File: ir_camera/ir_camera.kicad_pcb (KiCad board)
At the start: 2 copper layers, 43.6 x 54.3 mm, 23 parts, among them J1 PowerIn, J2 Screen, U1 L7805, U2 ATMEGA328P-PU, U3 LD1117, U4 pixart_ir, Y1 Crystal_4pin, Y2 Crystal

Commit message: IR Camera v0.2
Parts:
- moved R1 7.53 mm to (180.0, 72.9), turned to -90 degrees
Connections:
- U4 pad 5: SLC -> SCL
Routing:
- net SCL: track 45.4 -> 75.1 mm
- net 4.5V: track 103.9 -> 97.7 mm
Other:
- board text added: "IR Camera v0.2 M.I.A.R. Labs nick.groesz@gmail.com"
- board text removed: "IR Camera v0.1 M.I.A.R. Labs nick.groesz@gmail.com"
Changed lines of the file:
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@@
 	(net 29 "unconnected-(U2-(PCINT4{slash}MISO)PB4-Pad18)")
 	(net 30 "unconnected-(U4-NC-Pad4)")
-	(net 31 "SLC")
-	(net 32 "Net-(U4-CLK)")
-	(net 33 "unconnected-(Y1-NC-Pad1)")
+	(net 31 "Net-(U4-CLK)")
+	(net 32 "unconnected-(Y1-NC-Pad1)")
 	(footprint "custom:pixart_ir"
 		(layer "F.Cu")
@@
 			(layers "*.Cu" "*.Mask")
 			(remove_unused_layers no)
-			(net 31 "SLC")
+			(net 8 "SCL")
 			(pinfunction "SLC")
 			(pintype "input")
@@
 			(layers "*.Cu" "*.Mask")
 			(remove_unused_layers no)
-			(net 32 "Net-(U4-CLK)")
+			(net 31 "Net-(U4-CLK)")
 			(pinfunction "CLK")
 			(pintype "input")
@@
 	(footprint "Resistor_THT:R_Axial_DIN0207_L6.3mm_D2.5mm_P7.62mm_Horizontal"
 		(layer "F.Cu")
-		(at 180.7 80.4 90)
+		(at 180 72.9 -90)
 		(descr "Resistor, Axial_DIN0207 series, Axial, Horizontal, pin pitch=7.62mm, 0.25W = 1/4W, length*diameter=6.3*2.5mm^2, http://cdn-reichelt.de/documents/datenblatt/B400/1_4W%23YAG.pdf")
 		(tags "Resistor Axial_DIN0207 series Axial Horizontal pin pitch 7.62mm 0.25W = 1/4W length 6.3mm diameter 2.5mm")
@@
 		)
 		(property "Datasheet" ""
-			(at 0 0 90)
+			(at 0 0 270)
 			(unlocked yes)
 			(layer "F.Fab")
@@
 		)
 		(property "Description" ""
-			(at 0 0 90)
+			(at 0 0 270)
 			(unlocked yes)
 			(layer "F.Fab")
@@
 		(attr through_hole)
 		(fp_line
-			(start 7.08 -1.37)
-			(end 7.08 -1.04)
+			(start 0.54 1.37)
+			(end 7.08 1.37)
 			(stroke
 				(width 0.12)
@@
 		)
 		(fp_line
-			(start 0.54 -1.37)
-			(end 7.08 -1.37)
+			(start 7.08 1.37)
+			(end 7.08 1.04)
 			(stroke
 				(width 0.12)
@@
 		)
 		(fp_line
-			(start 0.54 -1.04)
-			(end 0.54 -1.37)
+			(start 0.54 1.04)
+			(end 0.54 1.37)
 			(stroke
 				(width 0.12)
@@
 		)
 		(fp_line
-			(start 0.54 1.04)
-			(end 0.54 1.37)
+			(start 0.54 -1.04)
+			(end 0.54 -1.37)
 			(stroke
 				(width 0.12)
@@
 		)
 		(fp_line
-			(start 7.08 1.37)
-			(end 7.08 1.04)
+			(start 0.54 -1.37)
+			(end 7.08 -1.37)
 			(stroke
 				(width 0.12)
@@
 		)
 		(fp_line
-			(start 0.54 1.37)
-			(end 7.08 1.37)
+			(start 7.08 -1.37)
+			(end 7.08 -1.04)
 			(stroke
 				(width 0.12)
@@
 		)
 		(fp_line
-			(start 8.67 -1.5)
-			(end -1.05 -1.5)
+			(start -1.05 1.5)
+			(end 8.67 1.5)
 			(stroke
 				(width 0.05)
@@
 		)
 		(fp_line
-			(start -1.05 -1.5)
-			(end -1.05 1.5)
+			(start 8.67 1.5)
+			(end 8.67 -1.5)
 			(stroke
 				(width 0.05)
@@
 		)
 		(fp_line
-			(start 8.67 1.5)
-			(end 8.67 -1.5)
+			(start -1.05 -1.5)
+			(end -1.05 1.5)
 			(stroke
 				(width 0.05)
@@
 		)
 		(fp_line
-			(start -1.05 1.5)
-			(end 8.67 1.5)
+			(start 8.67 -1.5)
+			(end -1.05 -1.5)
 			(stroke
 				(width 0.05)
@@
 		)
 		(fp_line
-			(start 6.96 -1.25)
-			(end 0.66 -1.25)
+			(start 0.66 1.25)
+			(end 6.96 1.25)
 			(stroke
 				(width 0.1)
@@
 		)
 		(fp_line
-			(start 0.66 -1.25)
-			(end 0.66 1.25)
+			(start 6.96 1.25)
+			(end 6.96 -1.25)
 			(stroke
 				(width 0.1)
@@
 		)
 		(fp_line
-			(start 7.62 0)
-			(end 6.96 0)
+			(start 0 0)
+			(end 0.66 0)
 			(stroke
 				(width 0.1)
@@
 		)
 		(fp_line
-			(start 0 0)
-			(end 0.66 0)
+			(start 7.62 0)
+			(end 6.96 0)
 			(stroke
 				(width 0.1)
@@
 		)
 		(fp_line
-			(start 6.96 1.25)
-			(end 6.96 -1.25)
+			(start 0.66 -1.25)
+			(end 0.66 1.25)
 			(stroke
 				(width 0.1)
@@
 		)
 		(fp_line
-			(start 0.66 1.25)
-			(end 6.96 1.25)
+			(start 6.96 -1.25)
+			(end 0.66 -1.25)
 			(stroke
 				(width 0.1)
@@
 		)
 		(pad "1" thru_hole circle
-			(at 0 0 90)
+			(at 0 0 270)
 			(size 1.6 1.6)
 			(drill 0.8)
@@
 		)
 		(pad "2" thru_hole oval
-			(at 7.62 0 90)
+			(at 7.62 0 270)
 			(size 1.6 1.6)
 			(drill 0.8)
@@
 			(layers "*.Cu" "*.Mask")
 			(remove_unused_layers no)
-			(net 33 "unconnected-(Y1-NC-Pad1)")
+			(net 32 "unconnected-(Y1-NC-Pad1)")
 			(pinfunction "NC")
 			(pintype "passive+no_connect")
@@
 			(layers "*.Cu" "*.Mask")
 			(remove_unused_layers no)
-			(net 32 "Net-(U4-CLK)")
+			(net 31 "Net-(U4-CLK)")
 			(pinfunction "Output")
 			(pintype "passive")
@@
 		(layer "Edge.Cuts")
 	)
-	(gr_text "IR Camera v0.1\nM.I.A.R. Labs\nnick.groesz@gmail.com"
+	(gr_text "IR Camera v0.2\nM.I.A.R. Labs\nnick.groesz@gmail.com"
 		(at 169.5 79.3 90)
 		(layer "B.SilkS")
@@
 	)
 	(segment
-		(start 145.85 98.77)
-		(end 145.85 99)
-		(width 0.2)
-		(layer "F.Cu")
-		(net 2)
-	)
-	(segment
 		(start 159.1 114.5)
 		(end 159.8 113.8)
@@
 	)
 	(segment
-		(start 176.3 97.3)
-		(end 176.3 88)
+		(start 176.8 80.52)
+		(end 180 80.52)
 		(width 0.2)
 		(layer "B.Cu")
@@
 	)
 	(segment
-		(start 163.799 103.701)
-		(end 165 102.5)
+		(start 176.3 97.3)
+		(end 176.3 88)
 		(width 0.2)
 		(layer "B.Cu")
@@
 	)
 	(segment
-		(start 176.8 80.52)
-		(end 176.8 76.68)
+		(start 163.799 103.701)
+		(end 165 102.5)
 		(width 0.2)
 		(layer "B.Cu")
@@
 	)
 	(segment
-		(start 176.8 76.68)
-		(end 180.7 72.78)
-		(width 0.2)
-		(layer "B.Cu")
-		(net 3)
-	)
-	(segment
 		(start 153.58295 84.1)
 		(end 158.73295 89.25)
@@
 	)
 	(segment
-		(start 177.901 80.06395)
-		(end 177.901 80.15)
+		(start 163.183 67.6758)
+		(end 162.582 67.0748)
 		(width 0.2)
 		(layer "F.Cu")
@@
 	)
 	(segment
-		(start 180.45 80.15)
-		(end 180.7 80.4)
+		(start 174.8661 79.651)
+		(end 180 74.5171)
 		(width 0.2)
 		(layer "F.Cu")
@@
 	)
 	(segment
-		(start 176.34395 79.419)
-		(end 177.25605 79.419)
+		(start 163.391 79.651)
+		(end 174.8661 79.651)
 		(width 0.2)
 		(layer "F.Cu")
@@
 	)
 	(segment
-		(start 163.89 80.15)
-		(end 175.699 80.15)
+		(start 174.7758 67.6758)
+		(end 163.183 67.6758)
 		(width 0.2)
 		(layer "F.Cu")
@@
 	)
 	(segment
-		(start 177.25605 79.419)
-		(end 177.901 80.06395)
+		(start 180 72.9)
+		(end 174.7758 67.6758)
 		(width 0.2)
 		(layer "F.Cu")
@@
 	)
 	(segment
-		(start 175.699 80.06395)
-		(end 176.34395 79.419)
-		(width 0.2)
-		(layer "F.Cu")
-		(net 8)
-	)
-	(segment
-		(start 175.699 80.15)
-		(end 175.699 80.06395)
-		(width 0.2)
-		(layer "F.Cu")
-		(net 8)
-	)
-	(segment
-		(start 177.901 80.15)
-		(end 180.45 80.15)
+		(start 159.1 75.36)
+		(end 163.391 79.651)
 		(width 0.2)
 		(layer "F.Cu")
@@
 	)
 	(segment
-		(start 159.1 75.36)
-		(end 163.89 80.15)
+		(start 180 74.5171)
+		(end 180 72.9)
 		(width 0.2)
 		(layer "F.Cu")
@@
 	)
 	(segment
-		(start 181.499999 81.199999)
-		(end 181.499999 98.400001)
+		(start 181.5 74.4)
+		(end 180 72.9)
 		(width 0.2)
 		(layer "B.Cu")
@@
 	)
 	(segment
-		(start 180.7 80.4)
-		(end 181.499999 81.199999)
+		(start 181.5 98.4)
+		(end 181.5 74.4)
 		(width 0.2)
 		(layer "B.Cu")
@@
 	)
 	(segment
-		(start 181.499999 98.400001)
-		(end 179.6 100.3)
+		(start 179.6 100.3)
+		(end 181.5 98.4)
 		(width 0.2)
 		(layer "B.Cu")
@@
 		(width 0.2)
 		(layer "B.Cu")
-		(net 32)
+		(net 31)
 	)
 	(segment
@@
 		(width 0.2)
 		(layer "B.Cu")
-		(net 32)
+		(net 31)
 	)
 	(segment
@@
 		(width 0.2)
 		(layer "B.Cu")
-		(net 32)
+		(net 31)
 	)
 	(segment
@@
 		(width 0.2)
 		(layer "B.Cu")
-		(net 32)
+		(net 31)
 	)
 	(embedded_fonts no)

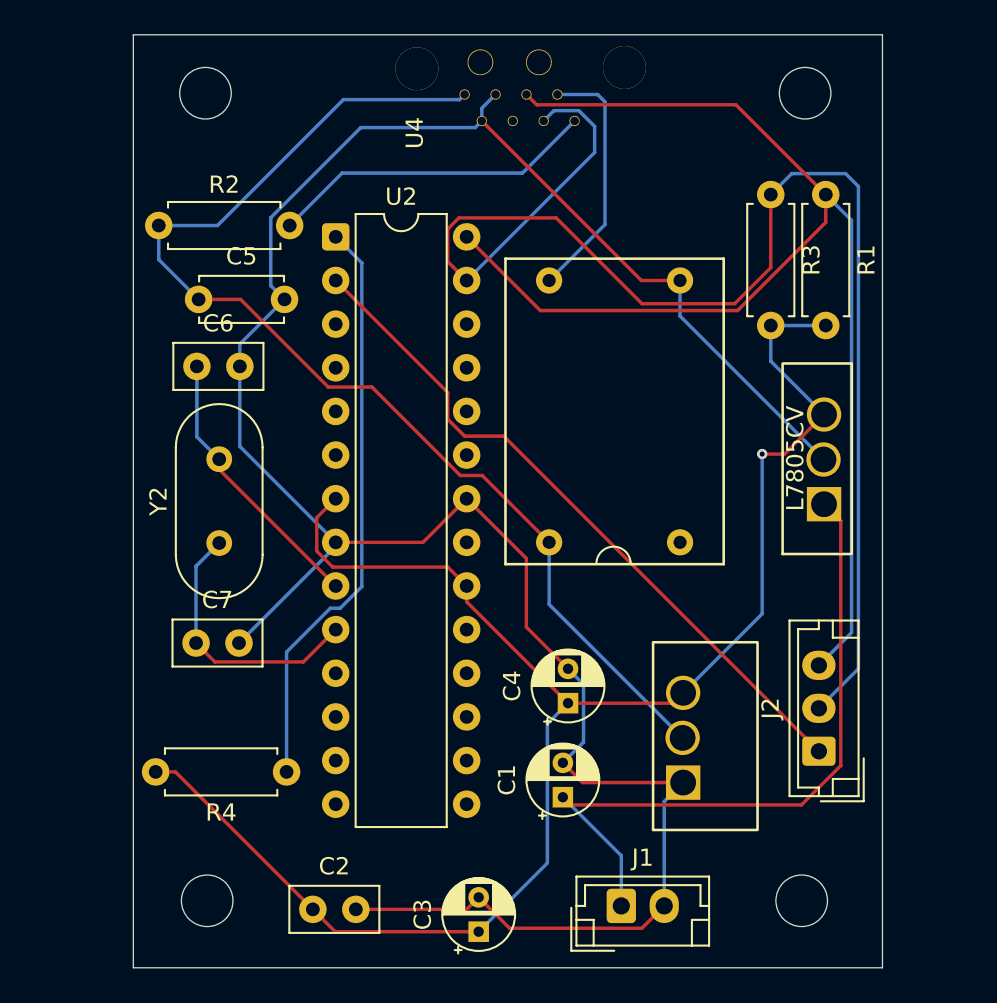
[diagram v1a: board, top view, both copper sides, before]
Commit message: IR Camera v0.2: add programming header
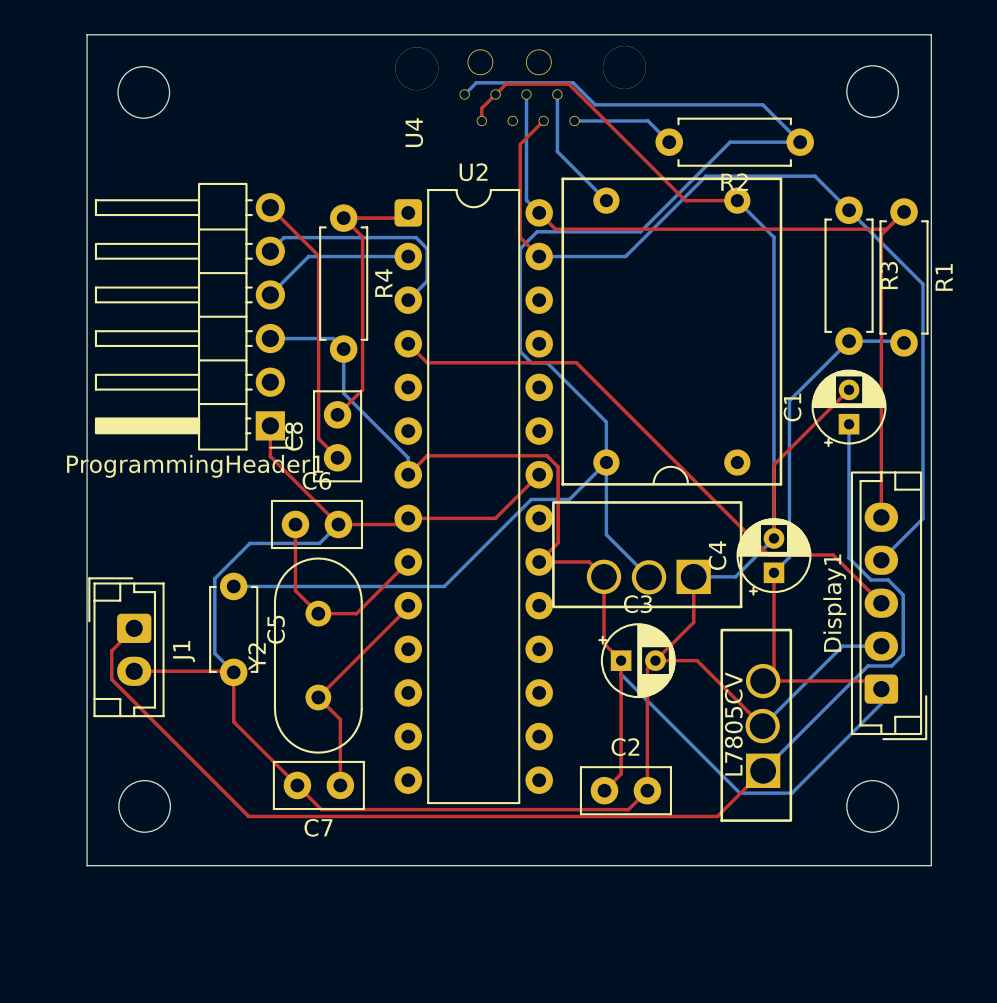
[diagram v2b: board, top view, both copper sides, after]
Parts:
- removed J2: Screen, Connector_JST:JST_EH_B3B-EH-A_1x03_P2.50mm_Vertical
- added C8: 100nF, Capacitor_THT:C_Disc_D5.0mm_W2.5mm_P2.50mm, F.Cu at (151.6, 88.2)
- added Display1: Conn_01x05_Pin, Connector_JST:JST_EH_B5B-EH-A_1x05_P2.50mm_Vertical, F.Cu at (183.2, 101.7)
- added ProgrammingHeader1: Programming Header, Connector_PinHeader_2.54mm:PinHeader_1x06_P2.54mm_Horizontal, F.Cu at (147.7, 86.4)
- moved R2 37.6 mm to (178.5, 69.8), turned to 180 degrees
- moved J1 32.6 mm to (139.8, 98.1), turned to -90 degrees
- moved R4 32.4 mm to (151.9, 74.3), turned to -90 degrees
- moved C1 27.4 mm to (181.4, 86.3)
- moved C2 18.3 mm to (167.1, 107.6)
- moved C3 17.8 mm to (168.1, 100.0), turned to 0 degrees
- moved C5 16.8 mm to (145.5, 95.7), turned to -90 degrees
- moved U1 15.9 mm to (175.4, 107.4)
- moved C4 14.2 mm to (177.0, 94.9)
- moved U3 12.3 mm to (173.3, 96.1), turned to 180 degrees
- moved C7 11.8 mm to (151.8, 107.3), turned to 180 degrees
- moved C6 10.8 mm to (149.1, 92.1)
- moved Y2 10.7 mm to (150.5, 102.2)
- moved H3 6.87 mm to (182.7, 108.5)
- moved H4 6.59 mm to (140.4, 108.5)
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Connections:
- U2 pad 2: Net-(J2-Pin_1) -> Rx
- U2 pad 3: unconnected-(U2-(PCINT17/TXD)PD1-Pad3) -> Tx
- U2 pad 4: unconnected-(U2-(PCINT18/INT0)PD2-Pad4) -> Net-(Display1-Pin_3)
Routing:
- net Net-(J2-Pin_1): track 40.4 -> 0.00 mm
- net Net-(Display1-Pin_3): track 0.00 -> 33.8 mm
- net 9V: track 40.7 -> 72.1 mm
- net SDA: track 82.6 -> 52.9 mm
- net SCL: track 75.1 -> 47.6 mm
- net 3.3V: track 67.1 -> 87.5 mm
- net Net-(U2-(PCINT14/~{RESET})PC6): track 33.9 -> 16.4 mm
- net GND: track 138.6 -> 155.8 mm
- net Net-(ProgrammingHeader1-Pin_6): track 0.00 -> 16.2 mm
- net Tx: track 0.00 -> 13.2 mm
- net Net-(U4-RESET): track 19.1 -> 6.02 mm
- net Rx: track 0.00 -> 8.95 mm
- net Net-(U4-CLK): track 14.7 -> 7.36 mm
- net Net-(U2-(PCINT6/XTAL1/TOSC1)PB6): track 16.1 -> 12.2 mm
- net Net-(U2-(PCINT7/XTAL2/TOSC2)PB7): track 15.7 -> 13.2 mm
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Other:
- board size 43.6 x 54.3 mm -> 49.1 x 48.4 mm
